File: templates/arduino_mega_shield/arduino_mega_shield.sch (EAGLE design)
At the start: 10 parts

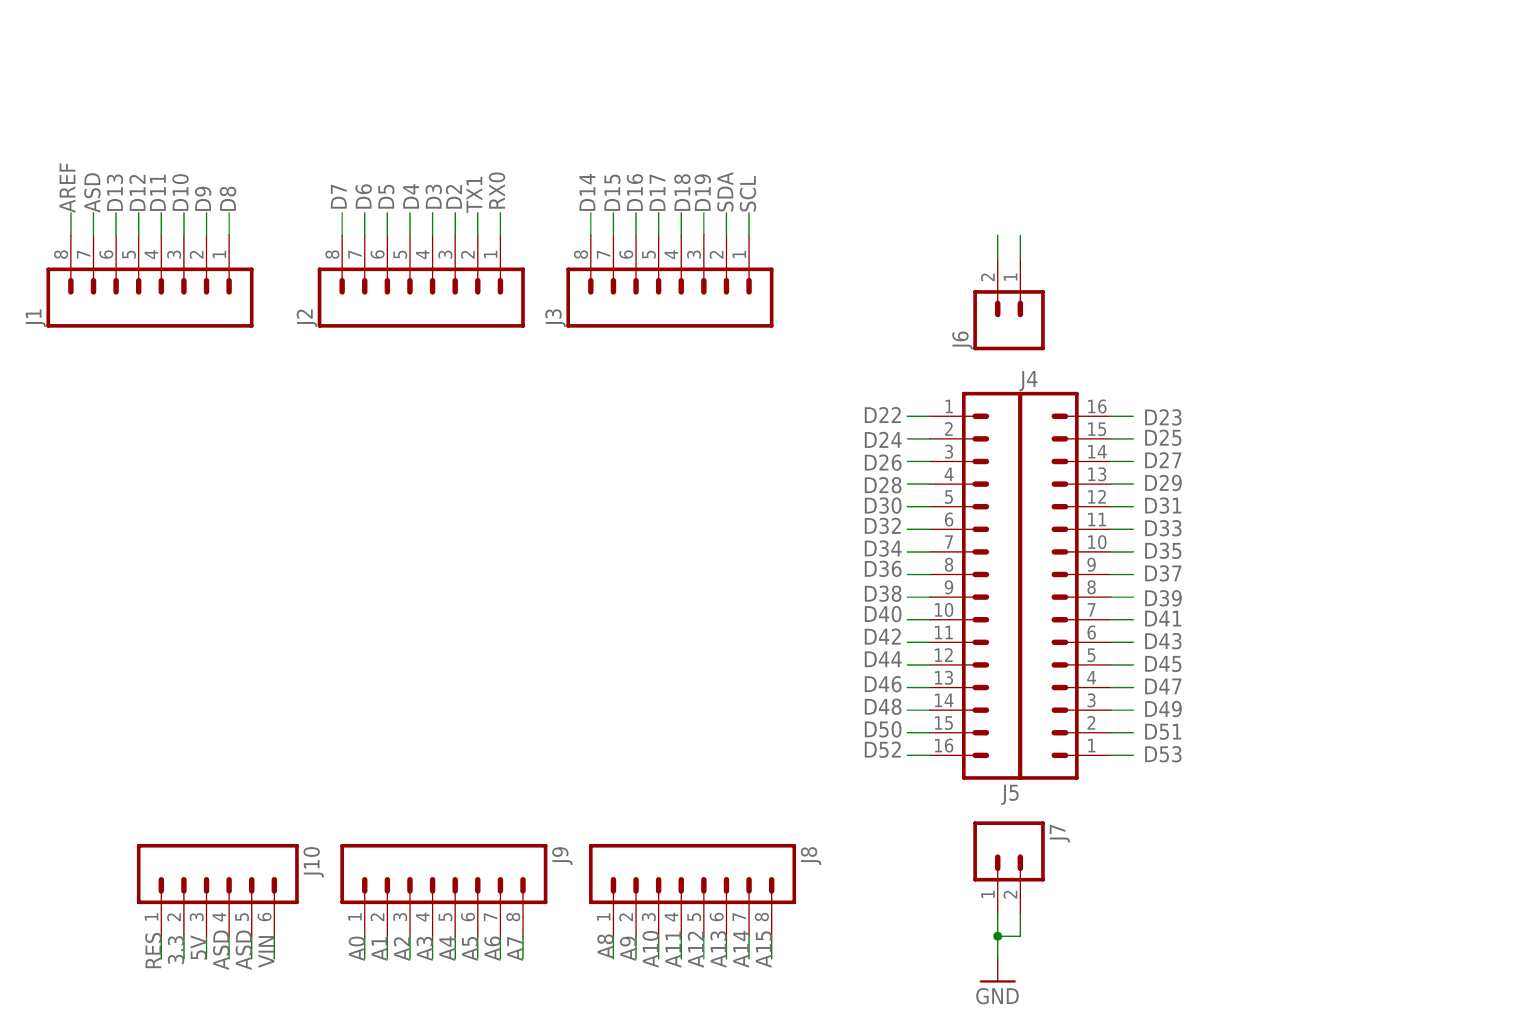
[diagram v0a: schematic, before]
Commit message: Fix GND en template mega
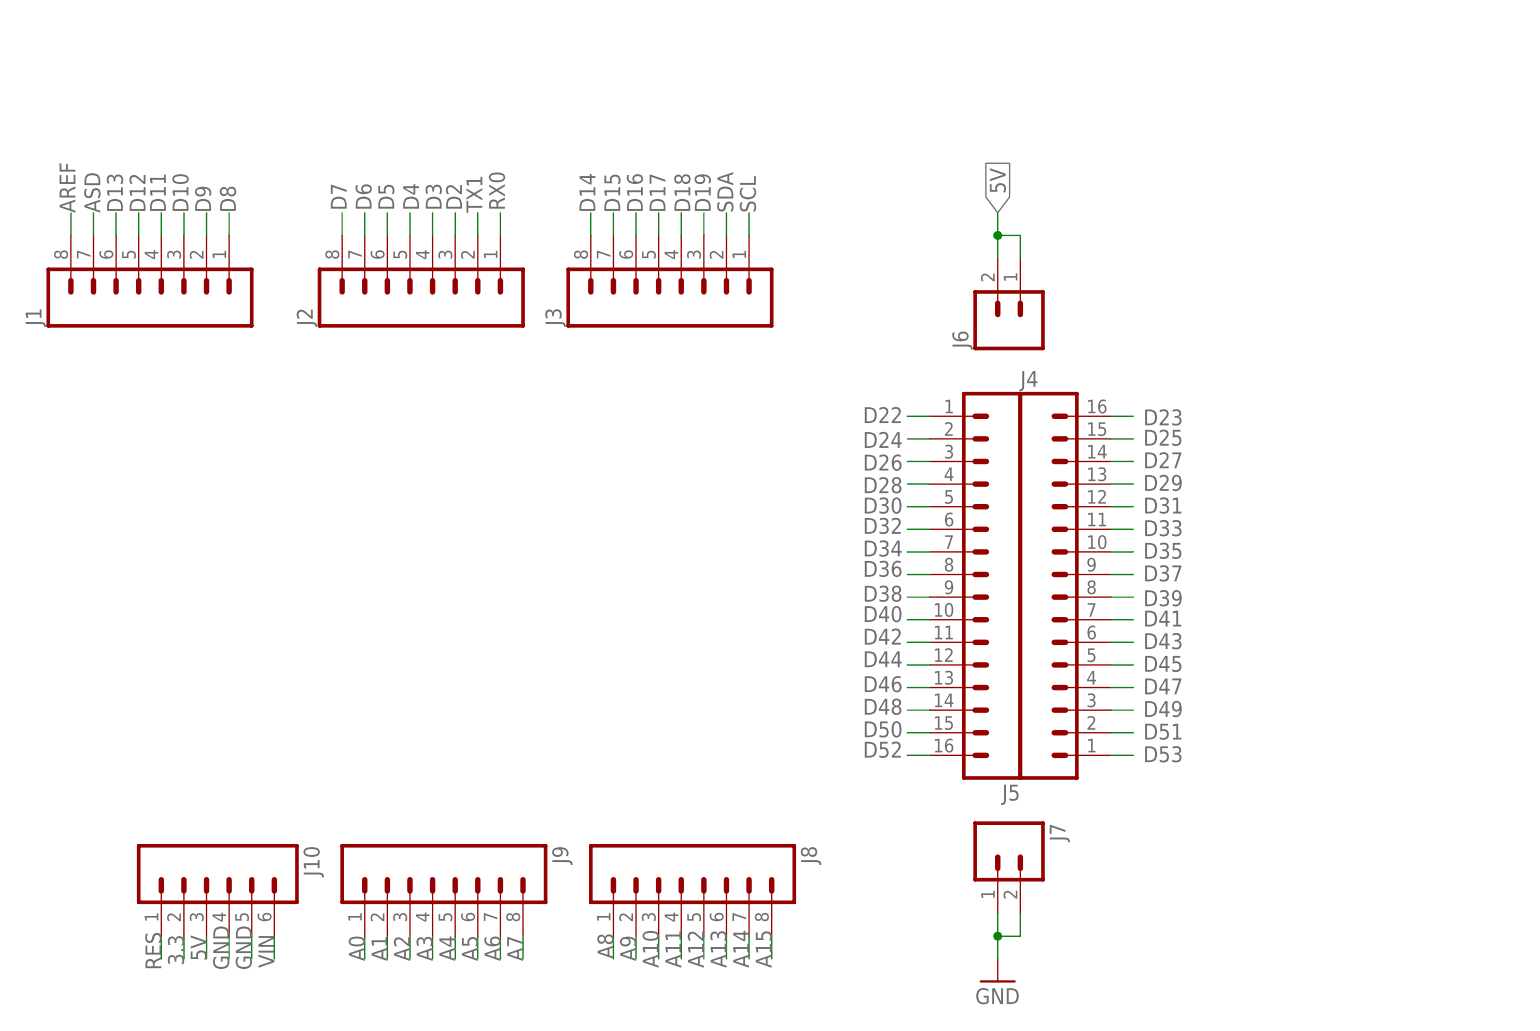
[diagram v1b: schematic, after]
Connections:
- removed net 5V@1: J6.1, J6.2
- new net GND: J10.4, J10.5, J7.1, J7.2
- net 5V: now also J6.1, J6.2
- net ASD: no longer J10.4, J10.5, J7.1, J7.2

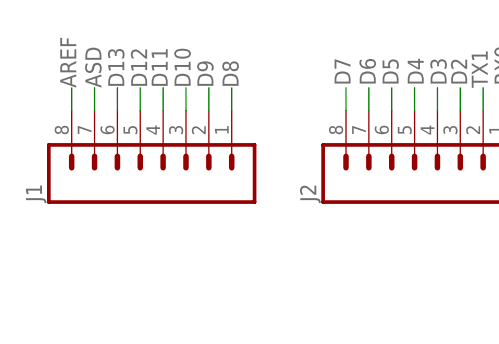
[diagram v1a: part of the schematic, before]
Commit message: Fix GND en template mega
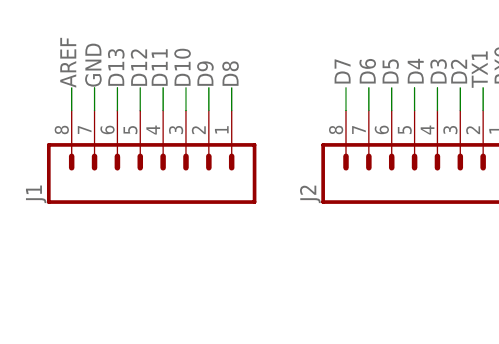
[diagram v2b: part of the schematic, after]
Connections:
- removed net ASD: J1.7
- net GND: now also J1.7
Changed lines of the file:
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@@
-</segment>
-</net>
-<net name="ASD" class="0">
-<segment>
-<wire x1="73.66" y1="134.62" x2="73.66" y2="137.16" width="0.1524" layer="91"/>
-<label x="74.422" y="137.16" size="1.778" layer="95" rot="R90"/>
-<pinref part="J1" gate="G$1" pin="7"/>
 </segment>
 </net>
@@
 <pinref part="J7" gate="G$1" pin="2"/>
 </segment>
-</net>
+<segment>
+<wire x1="73.66" y1="134.62" x2="73.66" y2="137.16" width="0.1524" layer="91"/>
+<label x="74.422" y="137.16" size="1.778" layer="95" rot="R90"/>
+<pinref part="J1" gate="G$1" pin="7"/>
+</segment>
+</net>

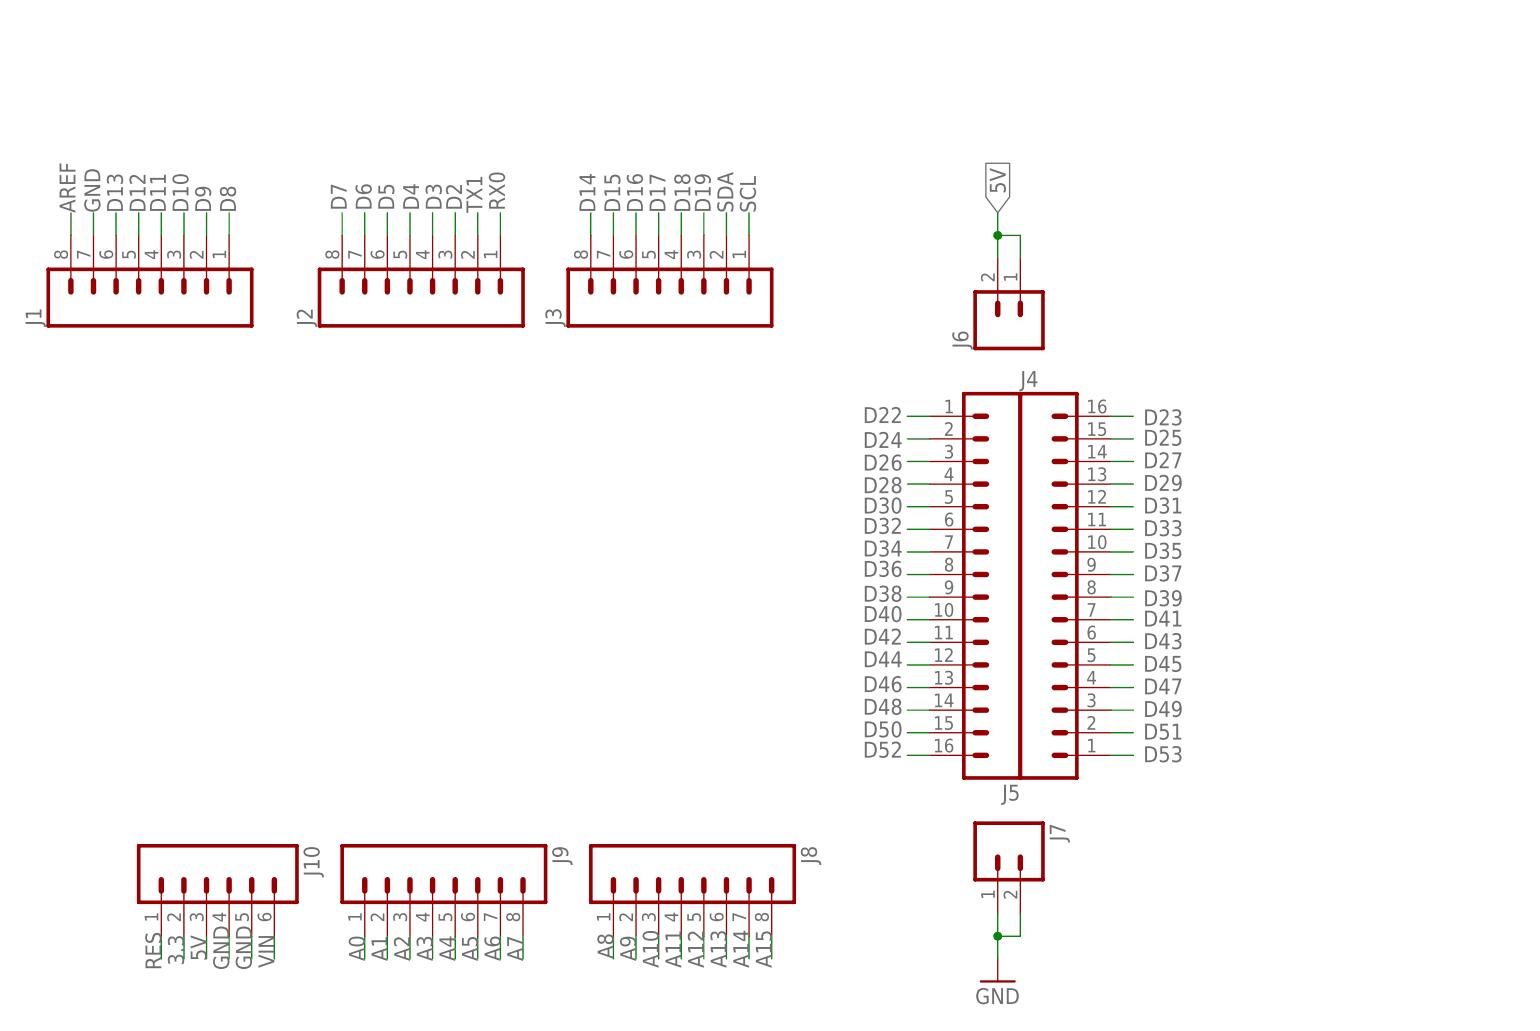
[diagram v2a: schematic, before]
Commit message: Update isolation and config for cnc
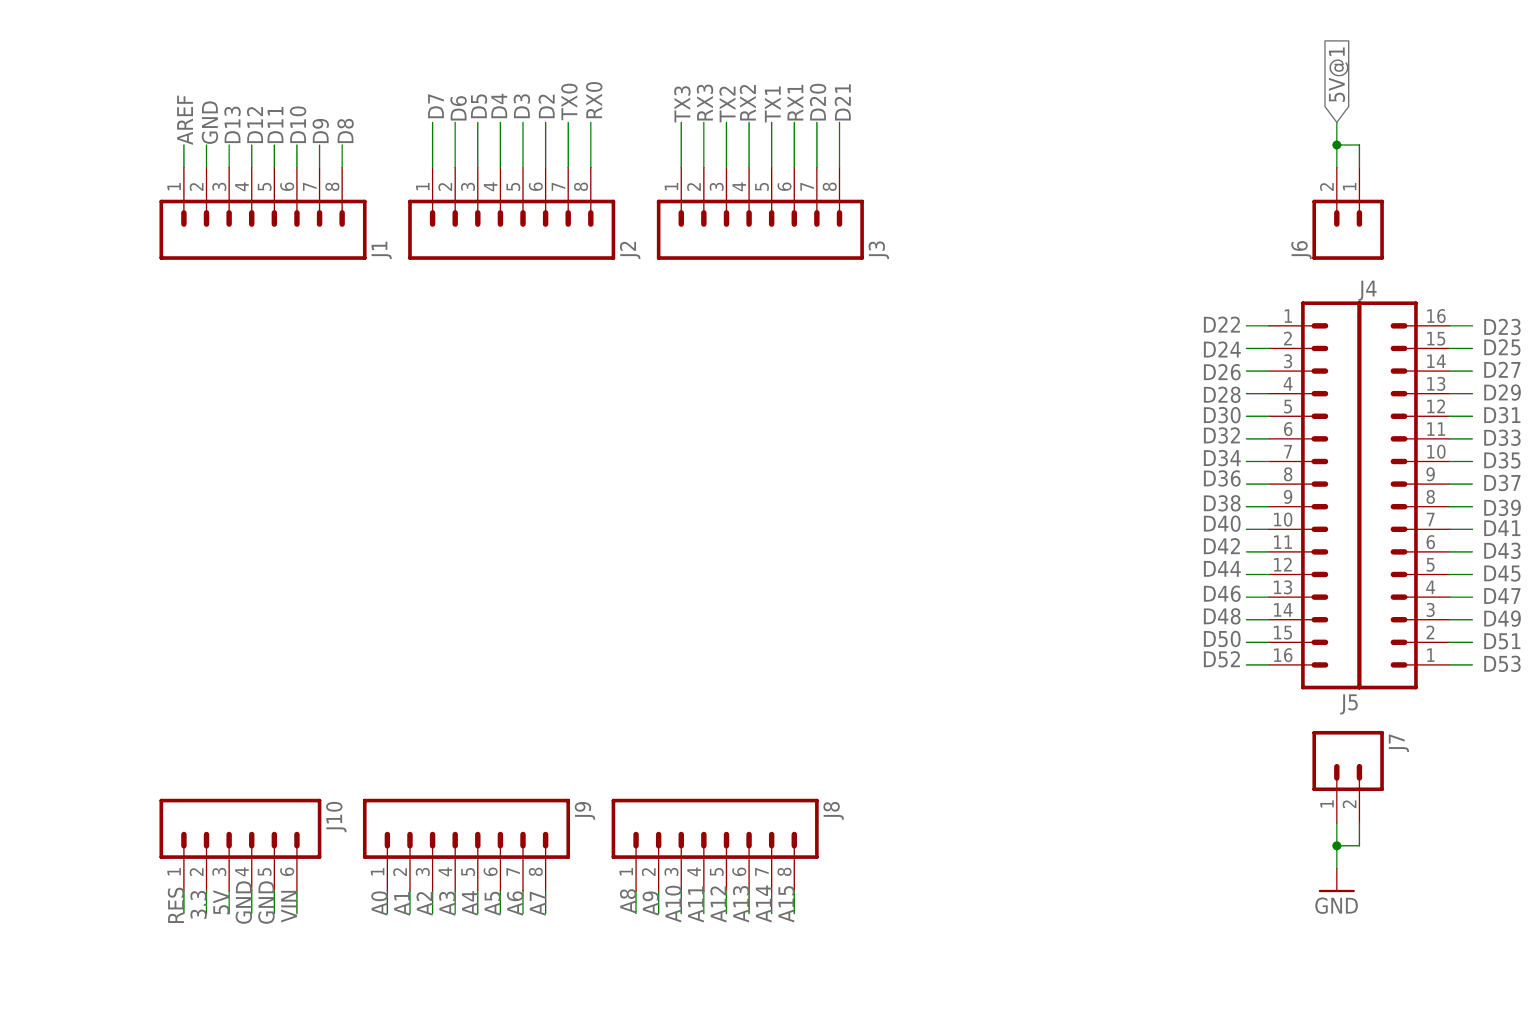
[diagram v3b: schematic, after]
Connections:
- net D14 renamed D21
- net D15 renamed D20
- net D16 renamed RX1
- net D18 renamed RX2
- net D19 renamed TX2
- net SCL renamed TX3
- net SDA renamed RX3
- removed net D17: J3.5
- new net 5V@1: J6.1, J6.2
- new net TX0: J2.7
- net 5V: no longer J6.1, J6.2
- net AREF: now also J1.1; no longer J1.8
- net D10: now also J1.6; no longer J1.3
- net D11: now also J1.5; no longer J1.4
- net D12: now also J1.4; no longer J1.5
- net D13: now also J1.3; no longer J1.6
- net D2: now also J2.6; no longer J2.3
- net D3: now also J2.5; no longer J2.4
- net D4: now also J2.4; no longer J2.5
- net D5: now also J2.3; no longer J2.6
- net D6: now also J2.2; no longer J2.7
- net D7: now also J2.1; no longer J2.8
- net D8: now also J1.8; no longer J1.1
- net D9: now also J1.7; no longer J1.2
- net GND: now also J1.2; no longer J1.7
- net RX0: now also J2.8; no longer J2.1
- net TX1: now also J3.5; no longer J2.2
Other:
- moved on the sheet: J1, J10, J2, J3, J4, J5, J6, J7, J8, J9
